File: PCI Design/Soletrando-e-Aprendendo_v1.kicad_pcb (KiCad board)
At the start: 2 copper layers, 115 x 115 mm, 47 parts, among them J1 I2C_Con, J2 I2C_Con, J3 I2C_Con, Q1 BC817, Q2 IRF9540N, SW1 Botão_A, SW2 Botão_B, SW3 ON/OFF, SW4 Cancel, SW5 Config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

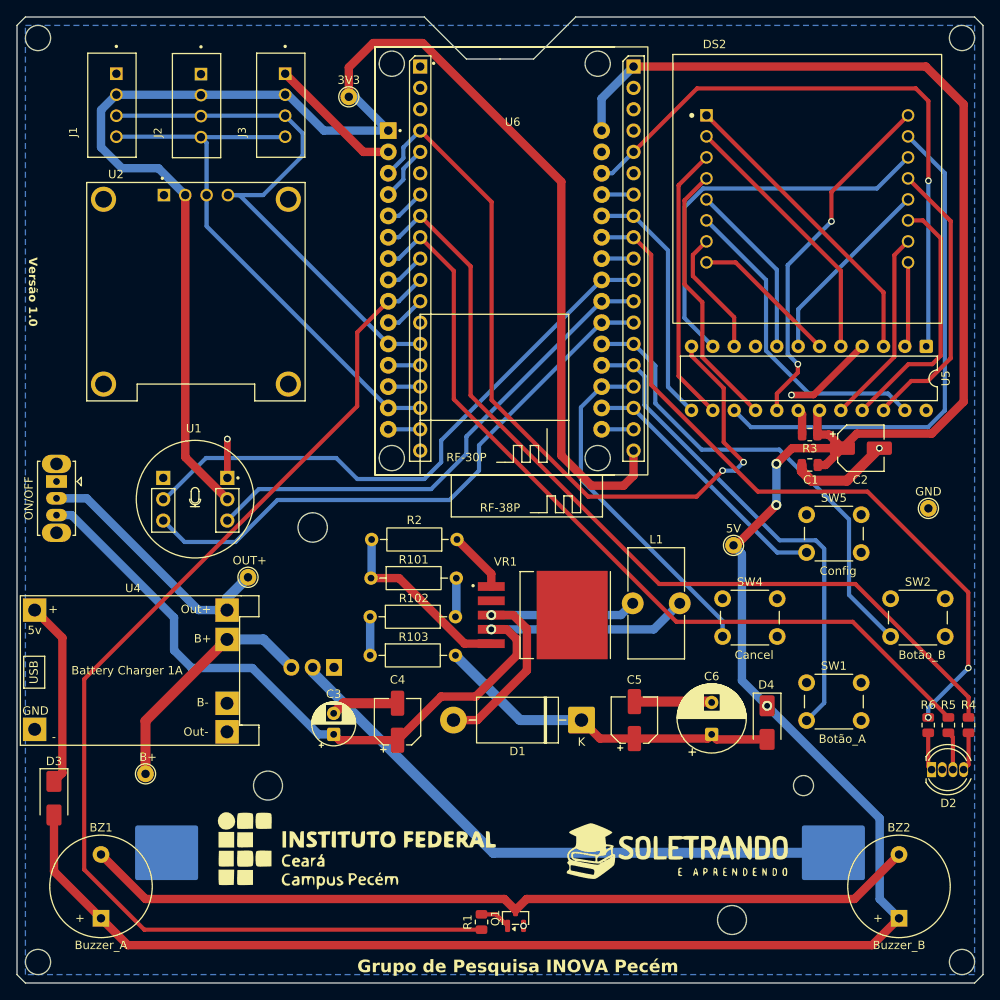
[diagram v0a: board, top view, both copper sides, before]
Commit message: Adicionando novos capacitores no circuito
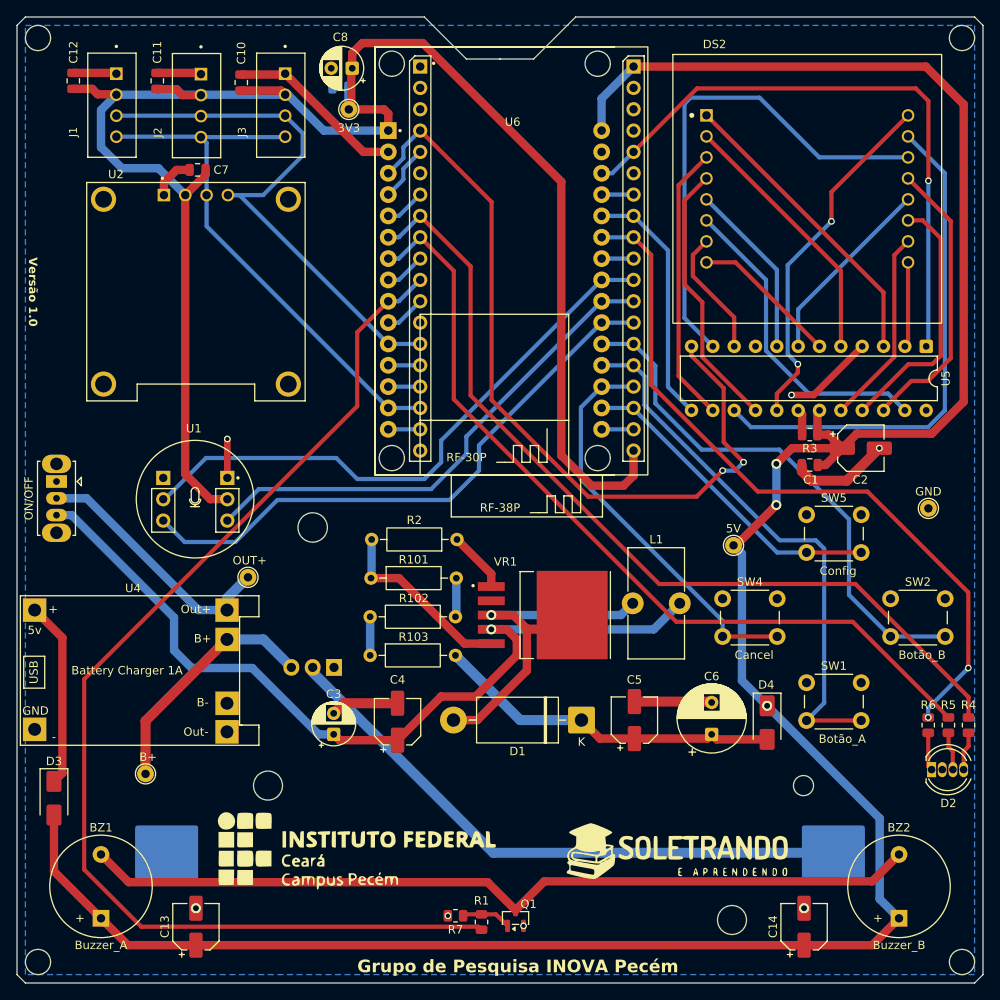
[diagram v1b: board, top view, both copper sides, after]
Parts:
- added C10: 100nF, Capacitor_SMD:C_0805_2012Metric, F.Cu at (104.2, 40.8)
- added C11: 100nF, Capacitor_SMD:C_0805_2012Metric, F.Cu at (94.2, 40.6)
- added C12: 100nF, Capacitor_SMD:C_0805_2012Metric, F.Cu at (84.2, 40.6)
- added C13: 10uF, Capacitor_SMD:CP_Elec_5x5.4, F.Cu at (98.8, 141.3)
- added C14: 10uF/16V, Capacitor_SMD:CP_Elec_5x5.4, F.Cu at (171.2, 141.3)
- added C7: 100nF, Capacitor_SMD:C_0805_2012Metric, F.Cu at (99.0, 51.2)
- added C8: 100uF/16V, Capacitor_THT:CP_Radial_D5.0mm_P2.50mm, F.Cu at (117.4, 39.1)
- added C9: 100nF, Capacitor_SMD:C_0805_2012Metric, B.Cu at (116.0, 41.4)
- added R7: 10K, Resistor_SMD:R_0805_2012Metric, F.Cu at (129.7, 140.0)
- C2: value 10uF/25V -> 10uF/16V
- C6: value 220uF/16V -> 470uF/16V
- U4: value TP4056-18650 -> TP4056-Module
- moved TP2 1.50 mm to (117.0, 44.0)
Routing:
- net +3V3: track 181.2 -> 208.2 mm
- net GNDREF: track 68.2 -> 89.1 mm, vias 4 -> 7
- net /DIG1: track 47.1 -> 60.1 mm
- net Net-(U6-SENSOR_VP): track 31.8 -> 38.3 mm
- net Net-(U6-SENSOR_VN): track 41.6 -> 48.1 mm
- net Net-(U6-IO35): track 56.7 -> 63.2 mm
- net Net-(U6-IO34): track 58.9 -> 65.4 mm
- net Net-(D1-A): track 38.5 -> 44.6 mm
- net Net-(Q1-B): track 3.67 -> 5.93 mm

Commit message: Adicionando novas serigrafias
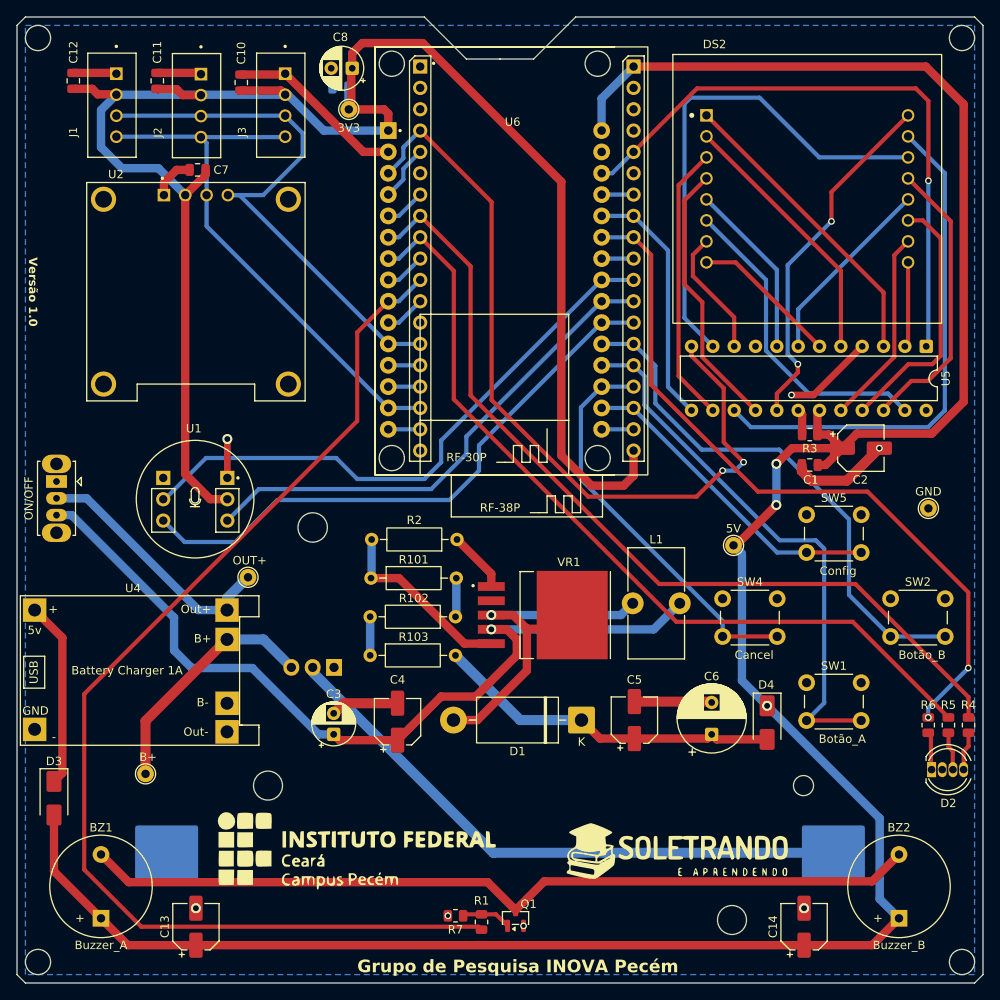
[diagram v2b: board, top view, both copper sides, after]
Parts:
- added G***: LOGO, LOGO:inova_pecem_34mm, B.Cu at (99.1, 65.4)
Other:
- board text added: "Autoria:"
- board text added: "Kauã L. Queiroz"
- board text added: "Luana S. M. Santos"
- board text added: "Tiago S. Façanha"
